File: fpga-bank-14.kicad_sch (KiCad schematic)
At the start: 20 parts, among them Q4 BSS138PW, Q5 BSS138PW, Q6 BSS138PW, Q7 BSS138PW, Q8 BSS138PW, U4 XC7K160T-FFG676

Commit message: [#86301] Project refresh 81589
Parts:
- R22: DNP DNP -> (none)

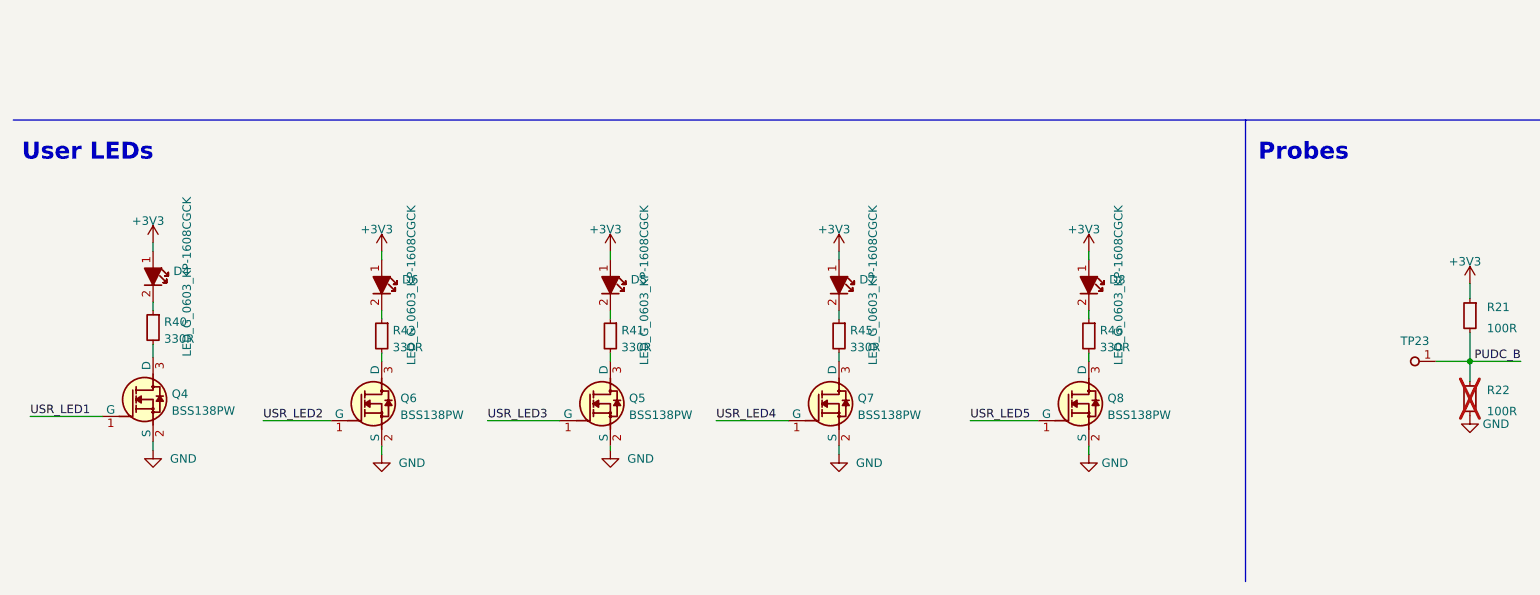
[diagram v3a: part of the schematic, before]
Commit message: [#87036] Update BSS138 transistors
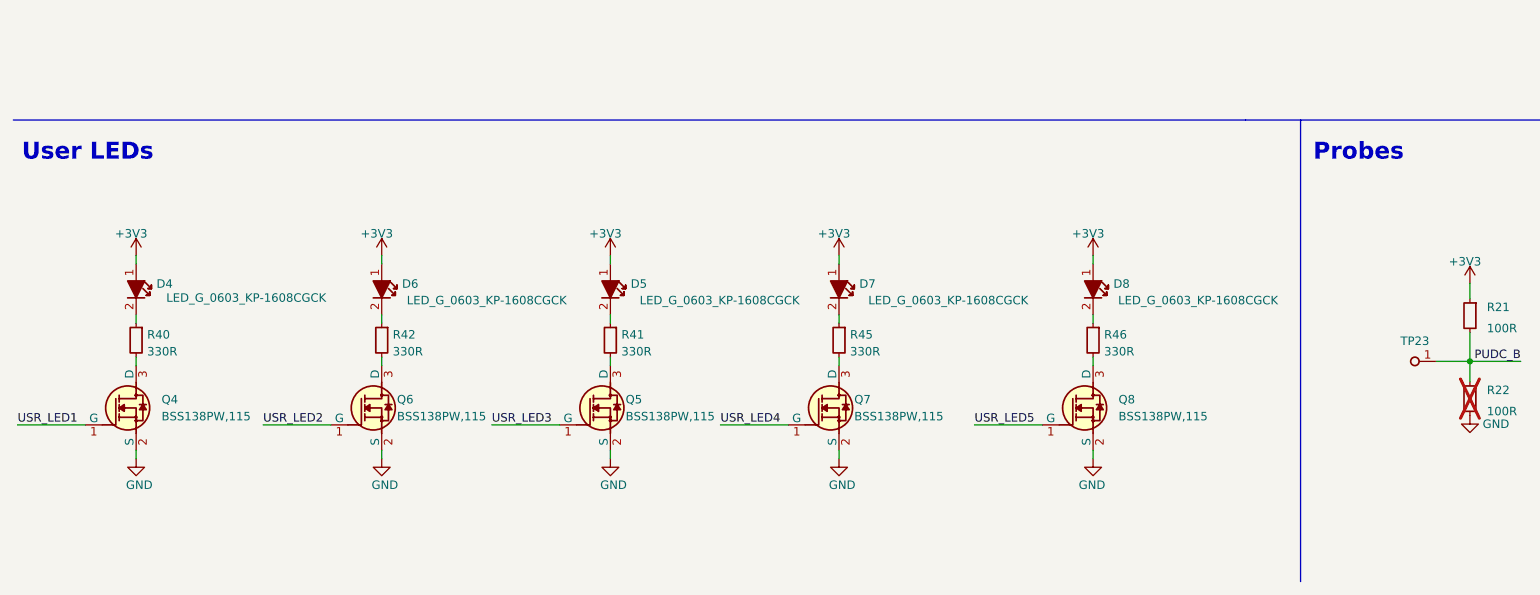
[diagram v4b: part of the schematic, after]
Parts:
- removed Q4, Q5, Q6, Q7, Q8: BSS138PW, antmicro-footprints:SC70-3, symbol antmicroTransistorsFETsMOSFETsSingle:BSS138PW
- added Q4, Q5, Q6, Q7, Q8: BSS138PW,115, antmicro-footprints:SC70-3, symbol antmicroTransistorsFETsMOSFETsSingle:BSS138PW,115
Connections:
- net GND: now also Q4.2 (S), Q5.2 (S), Q6.2 (S), Q7.2 (S), Q8.2 (S)
- net USR_LED1: now also Q4.1 (G)
- net USR_LED2: now also Q6.1 (G)
- net USR_LED3: now also Q5.1 (G)
- net USR_LED4: now also Q7.1 (G)
- net USR_LED5: now also Q8.1 (G)
- net at R45.2: now also Q7.3 (D)
- net at R40.2: now also Q4.3 (D)
- net at R46.2: now also Q8.3 (D)
- net at R41.2: now also Q5.3 (D)
- net at R42.2: now also Q6.3 (D)
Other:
- moved on the sheet: D4, D5, D6, D7, D8, R40, R41, R42, R45, R46

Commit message: [#87036] Add IC testpoints
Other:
- company: (none) -> Antmicro Ltd.
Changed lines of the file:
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@@
 	(title_block
 		(title "SO-DIMM DDR5 Tester")
-		(date "2025-11-25")
+		(date "2025-11-26")
 		(rev "1.3.0")
+		(company "Antmicro Ltd.")
 		(comment 1 "www.antmicro.com")
 		(comment 2 "Antmicro Ltd")
